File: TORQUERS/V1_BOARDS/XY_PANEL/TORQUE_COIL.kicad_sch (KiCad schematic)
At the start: 39 parts, among them Q1 BSS138, Q2 BSS138, Q4 BSS138, Q5 BSS138, U1 DRV8830DGQ

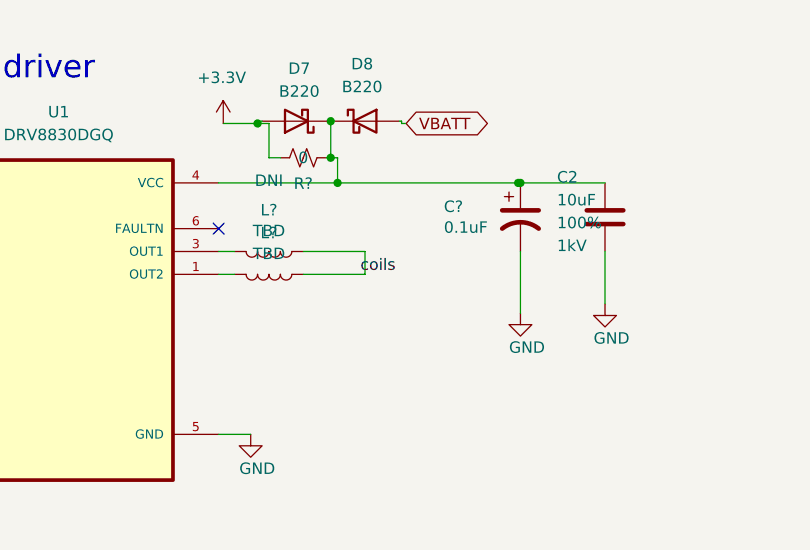
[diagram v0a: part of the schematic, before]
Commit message: Schematic lock on XY BOARD
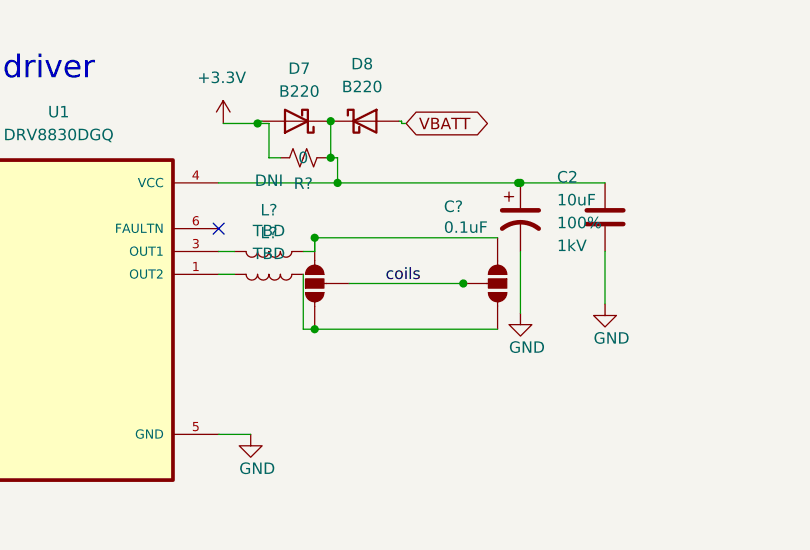
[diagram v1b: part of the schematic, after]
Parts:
- added JP2 (x2): ~, SparkFun-Jumper:SMT-JUMPER_3_NO_NO-SILK, symbol SparkFun-Jumper:SolderJumper_3_Open_No_Silk
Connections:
- net coils: now also JP2.2 (C), JP2.2 (C); no longer L?.1, L?.1
- new net: JP2.1 (A), JP2.3 (B), L?.1 (x2)
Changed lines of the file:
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@@
   (junction (at 127.254 71.374) (diameter 0) (color 0 0 0 0)
   )
+  (junction (at 133.604 94.234) (diameter 0) (color 0 0 0 0)
+  )
   (junction (at 247.396 51.816) (diameter 0) (color 0 0 0 0)
   )
@@
   (junction (at 135.382 71.12) (diameter 0) (color 0 0 0 0)
   )
+  (junction (at 150.114 89.154) (diameter 0) (color 0 0 0 0)
+  )
   (junction (at 73.66 85.598) (diameter 0) (color 0 0 0 0)
   )
@@
   (junction (at 234.696 48.006) (diameter 0) (color 0 0 0 0)
   )
+  (junction (at 133.604 84.074) (diameter 0) (color 0 0 0 0)
+  )
   (junction (at 252.476 23.876) (diameter 0) (color 0 0 0 0)
   )
@@
   )
   (no_connect (at 122.936 83.058))
+  (wire (pts (xy 132.334 94.234) (xy 133.604 94.234))
+    (stroke (width 0) (type default))
+  )
   (wire (pts (xy 122.936 105.918) (xy 126.492 105.918))
     (stroke (width 0) (type default))
@@
     (stroke (width 0) (type default))
   )
+  (wire (pts (xy 132.334 88.138) (xy 132.334 94.234))
+    (stroke (width 0) (type default))
+  )
   (wire (pts (xy 234.696 78.486) (xy 244.856 78.486))
     (stroke (width 0) (type default))
   )
-  (wire (pts (xy 139.192 85.598) (xy 139.192 88.138))
-    (stroke (width 0) (type default))
-  )
   (wire (pts (xy 244.856 65.786) (xy 242.316 65.786))
     (stroke (width 0) (type default))
   )
+  (wire (pts (xy 133.604 94.234) (xy 153.924 94.234))
+    (stroke (width 0) (type default))
+  )
   (wire (pts (xy 87.376 90.678) (xy 83.312 90.678))
     (stroke (width 0) (type default))
@@
     (stroke (width 0) (type default))
   )
+  (wire (pts (xy 133.604 84.074) (xy 153.924 84.074))
+    (stroke (width 0) (type default))
+  )
   (wire (pts (xy 244.856 48.006) (xy 234.696 48.006))
     (stroke (width 0) (type default))
@@
     (stroke (width 0) (type default))
   )
-  (wire (pts (xy 132.334 85.598) (xy 139.192 85.598))
-    (stroke (width 0) (type default))
-  )
   (wire (pts (xy 219.456 50.546) (xy 219.456 48.006))
     (stroke (width 0) (type default))
@@
     (stroke (width 0) (type default))
   )
+  (wire (pts (xy 133.604 85.598) (xy 133.604 84.074))
+    (stroke (width 0) (type default))
+  )
   (wire (pts (xy 134.874 75.184) (xy 135.382 75.184))
     (stroke (width 0) (type default))
@@
     (stroke (width 0) (type default))
   )
+  (wire (pts (xy 137.414 89.154) (xy 150.114 89.154))
+    (stroke (width 0) (type default))
+  )
   (wire (pts (xy 156.21 78.232) (xy 156.464 78.232))
     (stroke (width 0) (type default))
@@
     (stroke (width 0) (type default))
   )
+  (wire (pts (xy 150.114 89.154) (xy 150.114 89.408))
+    (stroke (width 0) (type default))
+  )
   (wire (pts (xy 219.456 70.866) (xy 224.536 70.866))
     (stroke (width 0) (type default))
@@
     (stroke (width 0) (type default))
   )
-  (wire (pts (xy 139.192 88.138) (xy 132.334 88.138))
+  (wire (pts (xy 132.334 85.598) (xy 133.604 85.598))
     (stroke (width 0) (type default))
   )
@@
     (effects (font (size 2.54 2.54)) (justify left bottom))
   )
-  (label "coils" (at 138.684 88.138 0) (fields_autoplaced)
+  (label "coils" (at 141.478 89.154 0) (fields_autoplaced)
     (effects (font (size 1.27 1.27)) (justify left bottom))
   )
@@
     )
   )
+  (symbol (lib_id "SparkFun-Jumper:SolderJumper_3_Open_No_Silk") (at 133.604 89.154 90) (unit 1)
+    (in_bom yes) (on_board yes) (dnp no) (fields_autoplaced)
+    (property "Reference" "JP2" (at 130.556 89.154 0)
+      (effects (font (size 1.27 1.27)) hide)
+    )
+    (property "Value" "~" (at 130.81 89.154 0)
+      (effects (font (size 1.27 1.27)))
+    )
+    (property "Footprint" "SparkFun-Jumper:SMT-JUMPER_3_NO_NO-SILK" (at 138.684 88.9 0)
+      (effects (font (size 1.27 1.27)) hide)
+    )
+    (property "Datasheet" "~" (at 139.954 89.154 0)
+      (effects (font (size 1.27 1.27)) hide)
+    )
+    (pin "1")
+    (pin "2")
+    (pin "3")
+    (instances
+      (project "Xpanel_V1_final"
+        (path "/97119169-578f-44be-8822-faf8f0e4fcd6"
+          (reference "JP2") (unit 1)
+        )
+        (path "/97119169-578f-44be-8822-faf8f0e4fcd6/db306d3f-1ab7-4e38-afab-c78bdb56c587"
+          (reference "JP2") (unit 1)
+        )
+        (path "/97119169-578f-44be-8822-faf8f0e4fcd6/06756695-4e8e-4b7d-905d-85546769f1f1"
+          (reference "JP2") (unit 1)
+        )
+        (path "/97119169-578f-44be-8822-faf8f0e4fcd6/6ee29482-1d20-4563-80a8-1ef8780df18b"
+          (reference "JP3") (unit 1)
+        )
+      )
+    )
+  )
   (symbol (lib_id "Device:R_US") (at 211.836 61.976 180) (unit 1)
     (in_bom yes) (on_board yes) (dnp no)
@@
         )
       )
+    )
+  )
+  (symbol (lib_id "SparkFun-Jumper:SolderJumper_3_Open_No_Silk") (at 153.924 89.154 270) (unit 1)
+    (in_bom yes) (on_board yes) (dnp no) (fields_autoplaced)
+    (property "Reference" "JP2" (at 156.972 89.154 0)
+      (effects (font (size 1.27 1.27)) hide)
+    )
+    (property "Value" "~" (at 156.718 89.154 0)
+      (effects (font (size 1.27 1.27)))
+    )
+    (property "Footprint" "SparkFun-Jumper:SMT-JUMPER_3_NO_NO-SILK" (at 148.844 89.408 0)
+      (effects (font (size 1.27 1.27)) hide)
+    )
+    (property "Datasheet" "~" (at 147.574 89.154 0)
+      (effects (font (size 1.27 1.27)) hide)
+    )
+    (pin "1")
+    (pin "2")
+    (pin "3")
+    (instances
+      (project "Xpanel_V1_final"
+        (path "/97119169-578f-44be-8822-faf8f0e4fcd6"
+          (reference "JP2") (unit 1)
+        )
+        (path "/97119169-578f-44be-8822-faf8f0e4fcd6/db306d3f-1ab7-4e38-afab-c78bdb56c587"
+          (reference "JP2") (unit 1)
+        )
+        (path "/97119169-578f-44be-8822-faf8f0e4fcd6/06756695-4e8e-4b7d-905d-85546769f1f1"
+          (reference "JP2") (unit 1)
+        )
+        (path "/97119169-578f-44be-8822-faf8f0e4fcd6/6ee29482-1d20-4563-80a8-1ef8780df18b"
+          (reference "JP4") (unit 1)
+        )
+      )

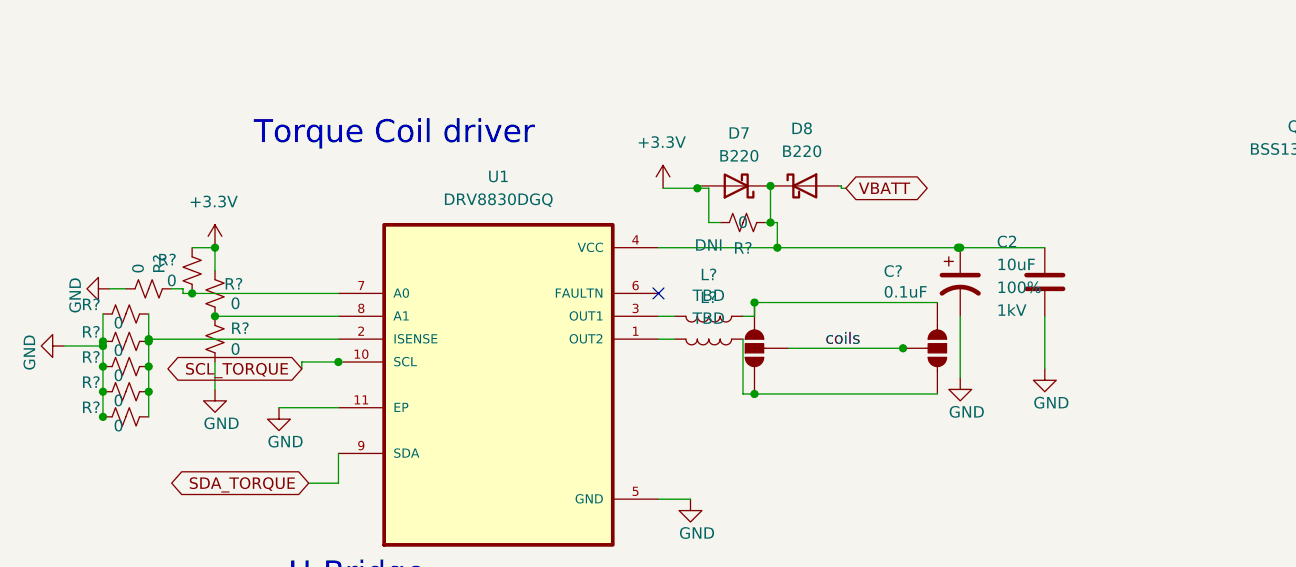
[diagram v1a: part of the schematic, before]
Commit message: completed XY Board
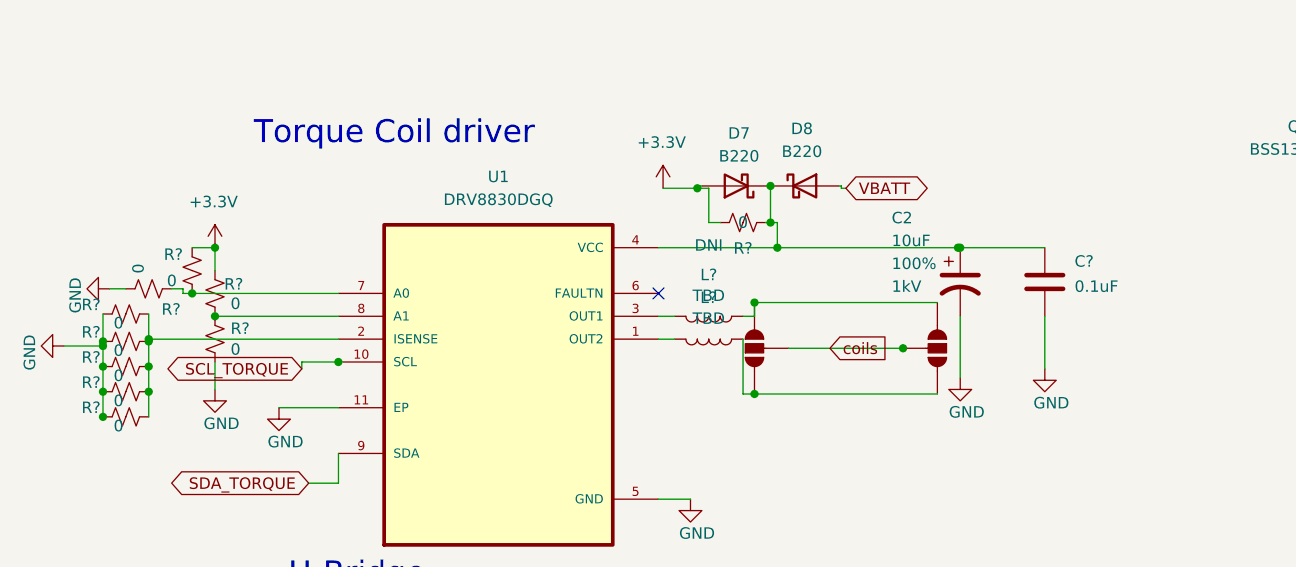
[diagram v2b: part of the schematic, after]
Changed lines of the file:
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@@
     (effects (font (size 2.54 2.54)) (justify left bottom))
-  )
-  (label "coils" (at 141.478 89.154 0) (fields_autoplaced)
-    (effects (font (size 1.27 1.27)) (justify left bottom))
   )
   (global_label "VBATT" (shape bidirectional) (at 143.764 71.374 0)
@@
     (property "Intersheetrefs" "${INTERSHEET_REFS}" (at 225.806 58.166 0)
       (effects (font (size 1.27 1.27)) hide)
+    )
+  )
+  (global_label "coils" (shape input) (at 141.986 89.154 0) (fields_autoplaced)
+    (effects (font (size 1.27 1.27)) (justify left))
+    (property "Intersheetrefs" "${INTERSHEET_REFS}" (at 149.5069 89.154 0)
+      (effects (font (size 1.27 1.27)) (justify left) hide)
     )
   )
@@
   (symbol (lib_id "Device:C") (at 165.862 81.788 0) (unit 1)
     (in_bom yes) (on_board yes) (dnp no)
-    (property "Reference" "C?" (at 147.955 80.6196 0)
-      (effects (font (size 1.27 1.27)) (justify left))
-    )
-    (property "Value" "0.1uF" (at 147.955 82.931 0)
+    (property "Reference" "C?" (at 169.164 79.502 0)
+      (effects (font (size 1.27 1.27)) (justify left))
+    )
+    (property "Value" "0.1uF" (at 169.164 82.296 0)
       (effects (font (size 1.27 1.27)) (justify left))
     )
@@
   (symbol (lib_id "Device:R_Small_US") (at 66.294 82.55 90) (unit 1)
     (in_bom yes) (on_board yes) (dnp no)
-    (property "Reference" "R?" (at 67.4624 80.8482 0)
+    (property "Reference" "R?" (at 69.85 84.836 90)
       (effects (font (size 1.27 1.27)) (justify left))
     )
@@
   )
   (symbol (lib_id "SparkFun-Capacitor:C_Polarized") (at 156.464 81.788 0) (unit 1)
-    (in_bom yes) (on_board yes) (dnp no) (fields_autoplaced)
-    (property "Reference" "C2" (at 160.528 77.343 0)
-      (effects (font (size 1.27 1.27)) (justify left))
-    )
-    (property "Value" "10uF" (at 160.528 79.883 0)
+    (in_bom yes) (on_board yes) (dnp no)
+    (property "Reference" "C2" (at 148.844 74.676 0)
+      (effects (font (size 1.27 1.27)) (justify left))
+    )
+    (property "Value" "10uF" (at 148.844 77.216 0)
       (effects (font (size 1.27 1.27)) (justify left))
     )
@@
       (effects (font (size 1.27 1.27)) hide)
     )
-    (property "Tolerance" "100%" (at 160.528 82.423 0)
-      (effects (font (size 1.27 1.27)) (justify left))
-    )
-    (property "Voltage" "1kV" (at 160.528 84.963 0)
+    (property "Tolerance" "100%" (at 148.844 79.756 0)
+      (effects (font (size 1.27 1.27)) (justify left))
+    )
+    (property "Voltage" "1kV" (at 148.844 82.296 0)
       (effects (font (size 1.27 1.27)) (justify left))
     )
@@
   (symbol (lib_id "Device:R_Small_US") (at 71.12 80.518 180) (unit 1)
     (in_bom yes) (on_board yes) (dnp no)
-    (property "Reference" "R?" (at 69.4182 79.3496 0)
-      (effects (font (size 1.27 1.27)) (justify left))
-    )
+    (property "Reference" "R?" (at 70.104 78.74 0)
+      (effects (font (size 1.27 1.27)) (justify left))
+    )

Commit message: made changes with feedback
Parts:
- removed L? (x2): TBD, Inductor_SMD:L_0603_1608Metric, symbol Device:L
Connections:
- net at JP2.1 (A), JP2.3 (B): now also U1.1 (OUT2)
- net at JP2.1 (A), JP2.3 (B): now also U1.3 (OUT1)
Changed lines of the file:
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@@
   (junction (at 61.214 96.774) (diameter 0) (color 0 0 0 0)
   )
+  (junction (at 136.652 94.234) (diameter 0) (color 0 0 0 0)
+  )
   (junction (at 211.836 78.486) (diameter 0) (color 0 0 0 0)
   )
@@
   (junction (at 257.556 70.866) (diameter 0) (color 0 0 0 0)
   )
+  (junction (at 136.652 84.074) (diameter 0) (color 0 0 0 0)
+  )
   (junction (at 61.214 93.98) (diameter 0) (color 0 0 0 0)
   )
@@
   (junction (at 127.254 71.374) (diameter 0) (color 0 0 0 0)
   )
-  (junction (at 133.604 94.234) (diameter 0) (color 0 0 0 0)
-  )
   (junction (at 247.396 51.816) (diameter 0) (color 0 0 0 0)
   )
@@
   (junction (at 234.696 48.006) (diameter 0) (color 0 0 0 0)
   )
-  (junction (at 133.604 84.074) (diameter 0) (color 0 0 0 0)
-  )
   (junction (at 252.476 23.876) (diameter 0) (color 0 0 0 0)
   )
@@
   )
   (no_connect (at 122.936 83.058))
-  (wire (pts (xy 132.334 94.234) (xy 133.604 94.234))
-    (stroke (width 0) (type default))
-  )
   (wire (pts (xy 122.936 105.918) (xy 126.492 105.918))
     (stroke (width 0) (type default))
@@
     (stroke (width 0) (type default))
   )
-  (wire (pts (xy 122.936 85.598) (xy 124.714 85.598))
+  (wire (pts (xy 122.936 85.598) (xy 133.604 85.598))
     (stroke (width 0) (type default))
   )
@@
     (stroke (width 0) (type default))
   )
-  (wire (pts (xy 133.604 94.234) (xy 153.924 94.234))
+  (wire (pts (xy 132.334 94.234) (xy 136.652 94.234))
     (stroke (width 0) (type default))
   )
@@
     (stroke (width 0) (type default))
   )
-  (wire (pts (xy 133.604 84.074) (xy 153.924 84.074))
-    (stroke (width 0) (type default))
-  )
   (wire (pts (xy 244.856 48.006) (xy 234.696 48.006))
     (stroke (width 0) (type default))
@@
     (stroke (width 0) (type default))
   )
-  (wire (pts (xy 137.414 89.154) (xy 150.114 89.154))
+  (wire (pts (xy 140.462 89.154) (xy 150.114 89.154))
     (stroke (width 0) (type default))
   )
@@
     (stroke (width 0) (type default))
   )
-  (wire (pts (xy 122.936 88.138) (xy 124.714 88.138))
+  (wire (pts (xy 122.936 88.138) (xy 132.334 88.138))
     (stroke (width 0) (type default))
   )
@@
     (stroke (width 0) (type default))
   )
+  (wire (pts (xy 136.652 84.074) (xy 133.604 84.074))
+    (stroke (width 0) (type default))
+  )
+  (wire (pts (xy 136.652 84.074) (xy 153.924 84.074))
+    (stroke (width 0) (type default))
+  )
   (wire (pts (xy 84.074 104.14) (xy 87.376 104.14))
     (stroke (width 0) (type default))
@@
     (stroke (width 0) (type default))
   )
-  (wire (pts (xy 132.334 85.598) (xy 133.604 85.598))
-    (stroke (width 0) (type default))
-  )
   (wire (pts (xy 61.214 88.392) (xy 61.214 88.9))
     (stroke (width 0) (type default))
@@
   )
   (wire (pts (xy 135.382 71.12) (xy 135.382 75.184))
+    (stroke (width 0) (type default))
+  )
+  (wire (pts (xy 136.652 94.234) (xy 153.924 94.234))
     (stroke (width 0) (type default))
   )
@@
     )
   )
-  (symbol (lib_id "SparkFun-Jumper:SolderJumper_3_Open_No_Silk") (at 133.604 89.154 90) (unit 1)
+  (symbol (lib_id "SparkFun-Jumper:SolderJumper_3_Open_No_Silk") (at 136.652 89.154 90) (unit 1)
     (in_bom yes) (on_board yes) (dnp no) (fields_autoplaced)
-    (property "Reference" "JP2" (at 130.556 89.154 0)
-      (effects (font (size 1.27 1.27)) hide)
-    )
-    (property "Value" "~" (at 130.81 89.154 0)
+    (property "Reference" "JP2" (at 133.604 89.154 0)
+      (effects (font (size 1.27 1.27)) hide)
+    )
+    (property "Value" "~" (at 133.858 89.154 0)
       (effects (font (size 1.27 1.27)))
     )
-    (property "Footprint" "SparkFun-Jumper:SMT-JUMPER_3_NO_NO-SILK" (at 138.684 88.9 0)
-      (effects (font (size 1.27 1.27)) hide)
-    )
-    (property "Datasheet" "~" (at 139.954 89.154 0)
+    (property "Footprint" "SparkFun-Jumper:SMT-JUMPER_3_NO_NO-SILK" (at 141.732 88.9 0)
+      (effects (font (size 1.27 1.27)) hide)
+    )
+    (property "Datasheet" "~" (at 143.002 89.154 0)
       (effects (font (size 1.27 1.27)) hide)
     )
@@
         (path "/97119169-578f-44be-8822-faf8f0e4fcd6/6ee29482-1d20-4563-80a8-1ef8780df18b"
           (reference "R25") (unit 1)
-        )
-      )
-    )
-  )
-  (symbol (lib_id "Device:L") (at 128.524 85.598 270) (unit 1)
-    (in_bom yes) (on_board yes) (dnp no)
-    (property "Reference" "L?" (at 128.524 81.0006 90)
-      (effects (font (size 1.27 1.27)))
-    )
-    (property "Value" "TBD" (at 128.524 83.312 90)
-      (effects (font (size 1.27 1.27)))
-    )
-    (property "Footprint" "Inductor_SMD:L_0603_1608Metric" (at 128.524 85.598 0)
-      (effects (font (size 1.27 1.27)) hide)
-    )
-    (property "Datasheet" "~" (at 128.524 85.598 0)
-      (effects (font (size 1.27 1.27)) hide)
-    )
-    (pin "1")
-    (pin "2")
-    (instances
-      (project "xpanel"
-        (path "/30bf83b4-3f3b-46f2-ac0f-8077e2dc1b24"
-          (reference "L?") (unit 1)
-        )
-      )
-      (project "Xpanel_V1_final"
-        (path "/97119169-578f-44be-8822-faf8f0e4fcd6"
-          (reference "L1") (unit 1)
-        )
-        (path "/97119169-578f-44be-8822-faf8f0e4fcd6/db306d3f-1ab7-4e38-afab-c78bdb56c587"
-          (reference "L1") (unit 1)
-        )
-        (path "/97119169-578f-44be-8822-faf8f0e4fcd6/6ee29482-1d20-4563-80a8-1ef8780df18b"
-          (reference "L1") (unit 1)
         )
       )
@@
         )
       )
-    )
-  )
-  (symbol (lib_id "Device:L") (at 128.524 88.138 270) (unit 1)
-    (in_bom yes) (on_board yes) (dnp no)
-    (property "Reference" "L?" (at 128.524 83.5406 90)
-      (effects (font (size 1.27 1.27)))
-    )
-    (property "Value" "TBD" (at 128.524 85.852 90)
-      (effects (font (size 1.27 1.27)))
-    )
-    (property "Footprint" "Inductor_SMD:L_0603_1608Metric" (at 128.524 88.138 0)
-      (effects (font (size 1.27 1.27)) hide)
-    )
-    (property "Datasheet" "~" (at 128.524 88.138 0)
-      (effects (font (size 1.27 1.27)) hide)
-    )
-    (pin "1")
-    (pin "2")
-    (instances
-      (project "xpanel"
-        (path "/30bf83b4-3f3b-46f2-ac0f-8077e2dc1b24"
-          (reference "L?") (unit 1)
-        )
-      )
-      (project "Xpanel_V1_final"
-        (path "/97119169-578f-44be-8822-faf8f0e4fcd6"
-          (reference "L2") (unit 1)
-        )
-        (path "/97119169-578f-44be-8822-faf8f0e4fcd6/db306d3f-1ab7-4e38-afab-c78bdb56c587"
-          (reference "L2") (unit 1)
-        )
-        (path "/97119169-578f-44be-8822-faf8f0e4fcd6/6ee29482-1d20-4563-80a8-1ef8780df18b"
-          (reference "L2") (unit 1)
-        )
-      )
